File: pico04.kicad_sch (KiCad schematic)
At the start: 41 parts

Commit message: Place the footprint on the PCB
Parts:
- removed C? (x4): 0.1uF, symbol Device:C_Small
- removed UGRGB? (x4): WS2812B, LED_SMD:LED_WS2812B_PLCC4_5.0x5.0mm_P3.2mm, symbol LED:WS2812B
- C1: renamed from C?; footprint (none) -> Capacitor_SMD:C_0805_2012Metric
- CRGB1, CRGB2, CRGB3, CRGB4: renamed from C?; footprint (none) -> Capacitor_SMD:C_0603_1608Metric
- D1, D2, D3, D4: renamed from D?; footprint (none) -> Diode_SMD:D_SOD-123
- MX1, MX2, MX3, MX4: renamed from MX?; footprint (none) -> Pico04:MXOnly-1U-Hotswap
- R3, R4, R5, R6: renamed from R?; footprint (none) -> Resistor_SMD:R_0805_2012Metric
- RGB1: renamed from RGB?; footprint LED_SMD:LED_WS2812B_PLCC4_5.0x5.0mm_P3.2mm -> Pico04:WS2812B-3528
- RGB2, RGB3, RGB4: renamed from D?; footprint LED_SMD:LED_WS2812B_PLCC4_5.0x5.0mm_P3.2mm -> Pico04:WS2812B-3528
- SW1: renamed from SW?; footprint (none) -> random-keyboard-parts.pretty:SKQGADE010
- U1: renamed from U?; footprint Random-keyboard-parts:SOT143B -> random-keyboard-parts.pretty:SOT143B
- gave numbers to parts that had none: 10
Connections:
- net GND: now also CRGB1.2, CRGB2.2, CRGB3.2, CRGB4.2
- no-connect marks 4 -> 3

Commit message: Complete the PCB
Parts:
- renumbered D3 to D1, D4 to D2, D1 to D3, D2 to D4, MX3 to MX1, MX4 to MX2, MX1 to MX3, MX2 to MX4
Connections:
- net COL0: now also U2.22 (PC7)
- net COL1: now also U2.9 (PD3)
- net ROW0: now also D1.1 (K), D2.1 (K), U2.25 (PC5); no longer D3.1 (K), D4.1 (K)
- net ROW1: now also D3.1 (K), D4.1 (K), U2.16 (PB2); no longer D1.1 (K), D2.1 (K)
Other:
- moved on the sheet: D1, D2, D3, D4, MX1, MX2, MX3, MX4
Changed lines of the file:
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@@
   (junction (at 241.3 31.75))
   (junction (at 260.35 31.75))
+  (no_connect (at 242.57 123.19))
   (no_connect (at 58.42 44.45))
-  (no_connect (at 242.57 123.19))
   (no_connect (at 58.42 29.21))
   (wire (pts (xy 46.355 79.375) (xy 46.355 83.185))
@@
     (effects (font (size 1.27 1.27)) (justify right))
   )
+  (global_label "ROW1" (shape input) (at 191.135 39.37 0)
+    (effects (font (size 1.27 1.27)) (justify left))
+  )
   (global_label "RGBLED" (shape input) (at 191.135 41.91 0)
     (effects (font (size 1.27 1.27)) (justify left))
   )
+  (global_label "ROW0" (shape input) (at 191.135 62.23 0)
+    (effects (font (size 1.27 1.27)) (justify left))
+  )
+  (global_label "COL0" (shape input) (at 191.135 67.31 0)
+    (effects (font (size 1.27 1.27)) (justify left))
+  )
+  (global_label "COL1" (shape input) (at 191.135 80.01 0)
+    (effects (font (size 1.27 1.27)) (justify left))
+  )
   (global_label "ROW0" (shape input) (at 228.6 44.45 180)
     (effects (font (size 1.27 1.27)) (justify right))
@@
   )
   (symbol (lib_id "power:GND") (at 234.95 134.62 0) (unit 1)
-    (property "Reference" "#PWR?" (id 0) (at 234.95 140.97 0)
+    (property "Reference" "#PWR0116" (id 0) (at 234.95 140.97 0)
       (effects (font (size 1.27 1.27)) hide)
     )
@@
   )
   (symbol (lib_id "Device:D_Small") (at 231.775 40.64 90) (unit 1)
-    (property "Reference" "D1" (id 0) (at 233.5531 39.4906 90)
+    (property "Reference" "D1" (id 0) (at 233.553 39.491 90)
       (effects (font (size 1.27 1.27)) (justify right))
     )
@@
   )
   (symbol (lib_id "Device:D_Small") (at 231.775 59.69 90) (unit 1)
-    (property "Reference" "D3" (id 0) (at 233.5531 58.5406 90)
+    (property "Reference" "D3" (id 0) (at 233.553 58.541 90)
       (effects (font (size 1.27 1.27)) (justify right))
     )
@@
   )
   (symbol (lib_id "Device:D_Small") (at 250.825 40.64 90) (unit 1)
-    (property "Reference" "D2" (id 0) (at 252.6031 39.4906 90)
+    (property "Reference" "D2" (id 0) (at 252.603 39.491 90)
       (effects (font (size 1.27 1.27)) (justify right))
     )
@@
   )
   (symbol (lib_id "Device:D_Small") (at 250.825 59.69 90) (unit 1)
-    (property "Reference" "D4" (id 0) (at 252.6031 58.5406 90)
+    (property "Reference" "D4" (id 0) (at 252.603 58.541 90)
       (effects (font (size 1.27 1.27)) (justify right))
     )
@@
   )
   (symbol (lib_id "MX_Alps_Hybrid:MX-NoLED") (at 237.49 33.02 0) (unit 1)
-    (property "Reference" "MX1" (id 0) (at 238.3755 27.4192 0)
+    (property "Reference" "MX1" (id 0) (at 238.375 27.419 0)
       (effects (font (size 1.524 1.524)))
     )
@@
   )
   (symbol (lib_id "MX_Alps_Hybrid:MX-NoLED") (at 237.49 52.07 0) (unit 1)
-    (property "Reference" "MX3" (id 0) (at 238.3755 46.4692 0)
+    (property "Reference" "MX3" (id 0) (at 238.375 46.469 0)
       (effects (font (size 1.524 1.524)))
     )
@@
   )
   (symbol (lib_id "MX_Alps_Hybrid:MX-NoLED") (at 256.54 33.02 0) (unit 1)
-    (property "Reference" "MX2" (id 0) (at 257.4255 27.4192 0)
+    (property "Reference" "MX2" (id 0) (at 257.425 27.419 0)
       (effects (font (size 1.524 1.524)))
     )
@@
   )
   (symbol (lib_id "MX_Alps_Hybrid:MX-NoLED") (at 256.54 52.07 0) (unit 1)
-    (property "Reference" "MX4" (id 0) (at 257.4255 46.4692 0)
+    (property "Reference" "MX4" (id 0) (at 257.425 46.469 0)
       (effects (font (size 1.524 1.524)))
     )
@@
     )
     (path "/1d2d9655-11b9-43b8-8ab6-612e24aa6fec"
-      (reference "#PWR?") (unit 1)
+      (reference "#PWR0116") (unit 1)
     )
     (path "/26bfde33-3b17-4dfa-b632-b75632d47ae7"
@@
       (reference "CRGB4") (unit 1)
     )
+    (path "/bd4ab8ad-2f65-4d8a-8d0d-c0821e4954a4"
+      (reference "D1") (unit 1)
+    )
+    (path "/40e942c4-856f-4481-9752-16af2cfdf79c"
+      (reference "D2") (unit 1)
+    )
     (path "/3ff054c0-d21f-48f0-bf05-8c876ae67903"
-      (reference "D1") (unit 1)
+      (reference "D3") (unit 1)
     )
     (path "/25c6b1f6-bc0a-40f6-83d3-4b08379c2571"
-      (reference "D2") (unit 1)
-    )
-    (path "/bd4ab8ad-2f65-4d8a-8d0d-c0821e4954a4"
-      (reference "D3") (unit 1)
-    )
-    (path "/40e942c4-856f-4481-9752-16af2cfdf79c"
       (reference "D4") (unit 1)
     )
@@
       (reference "F1") (unit 1)
     )
+    (path "/cea816e9-fe33-478f-83b6-8714a776833b"
+      (reference "MX1") (unit 1)
+    )
+    (path "/d35a3ce5-ec9f-41d8-9163-6e0433cc9ea7"
+      (reference "MX2") (unit 1)
+    )
     (path "/74801bab-9abf-47a8-a68b-5b4028d688b4"
-      (reference "MX1") (unit 1)
+      (reference "MX3") (unit 1)
     )
     (path "/de405e8f-3a87-4ab0-b6fb-c3378cb8c0db"
-      (reference "MX2") (unit 1)
-    )
-    (path "/cea816e9-fe33-478f-83b6-8714a776833b"
-      (reference "MX3") (unit 1)
-    )
-    (path "/d35a3ce5-ec9f-41d8-9163-6e0433cc9ea7"
       (reference "MX4") (unit 1)
     )

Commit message: Add some 3d models to the PCB
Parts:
- F1: footprint Fuse:Fuse_1206_3216Metric -> Pico04:Fuse_1206_3216Metric
- USB1: footprint Type-C:HRO-TYPE-C-31-M-12 -> Pico04:HRO-TYPE-C-31-M-12
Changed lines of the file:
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@@
   (junction (at 260.35 31.75))
   (no_connect (at 242.57 123.19))
+  (no_connect (at 58.42 29.21))
   (no_connect (at 58.42 44.45))
-  (no_connect (at 58.42 29.21))
   (wire (pts (xy 46.355 79.375) (xy 46.355 83.185))
     (stroke (width 0) (type solid) (color 0 0 0 0))
@@
     (property "Reference" "F1" (id 0) (at 89.535 21.5708 90))
     (property "Value" "500mA" (id 1) (at 89.535 23.87 90))
-    (property "Footprint" "Fuse:Fuse_1206_3216Metric" (id 2) (at 94.615 25.4 0)
+    (property "Footprint" "Pico04:Fuse_1206_3216Metric" (id 2) (at 94.615 25.4 0)
       (effects (font (size 1.27 1.27)) (justify left) hide)
     )
@@
       (effects (font (size 1.524 1.524)))
     )
-    (property "Footprint" "Type-C:HRO-TYPE-C-31-M-12" (id 2) (at 55.88 38.1 0)
-      (effects (font (size 1.524 1.524)) hide)
-    )
+    (property "Footprint" "Pico04:HRO-TYPE-C-31-M-12" (id 2) (at 55.88 38.1 0)
+      (effects (font (size 1.524 1.524)) hide)
+    )

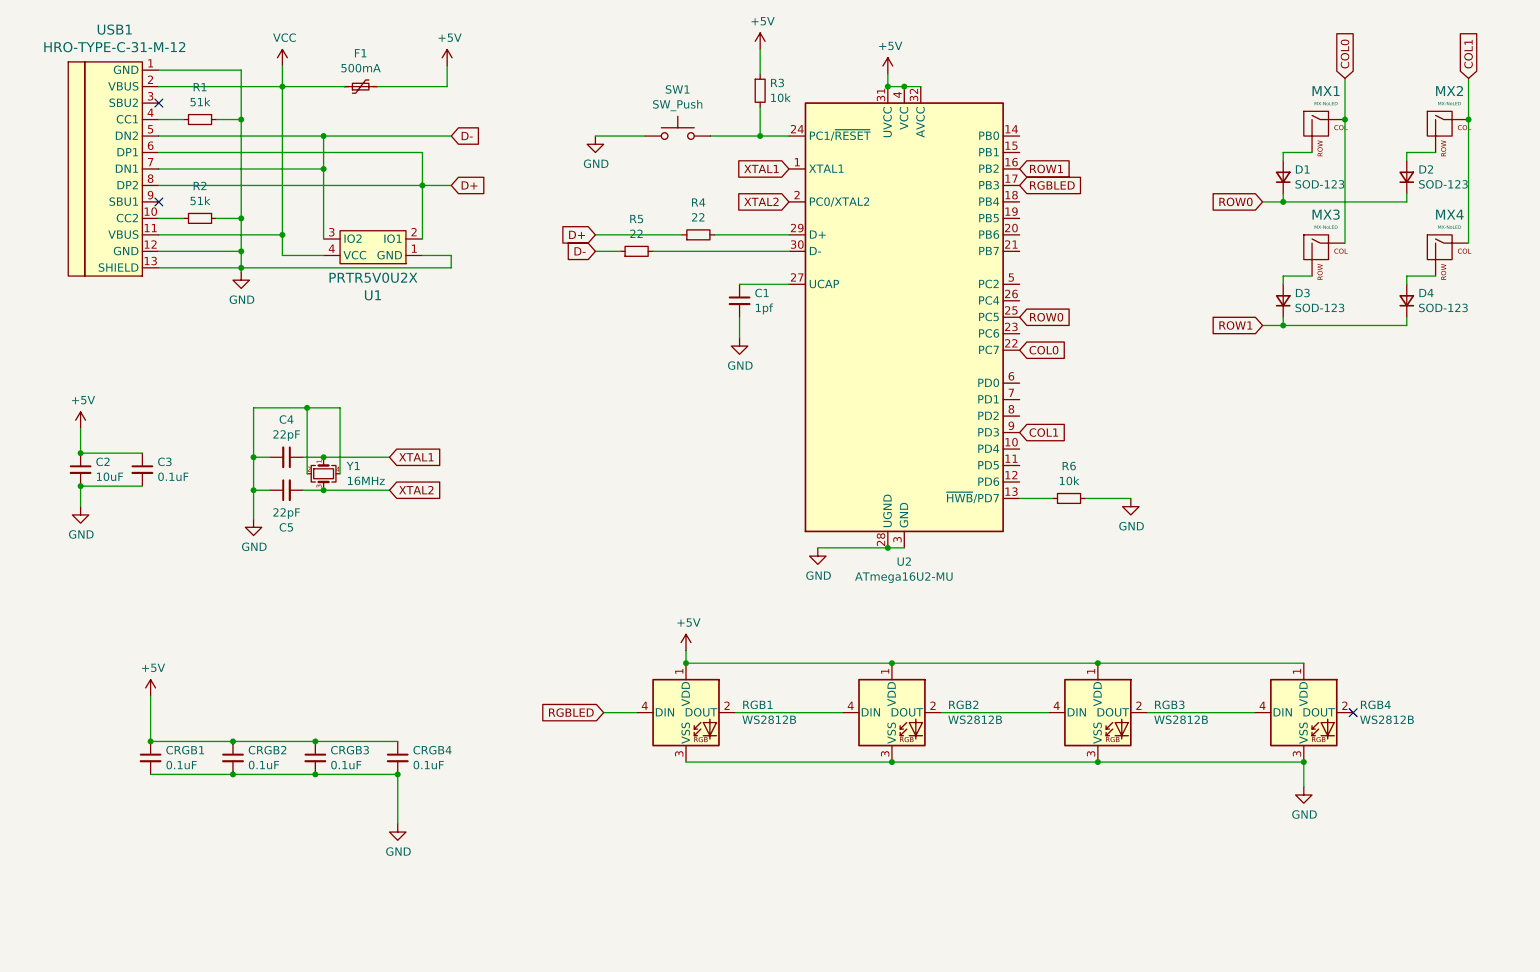
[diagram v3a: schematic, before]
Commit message: Re-route the PCB
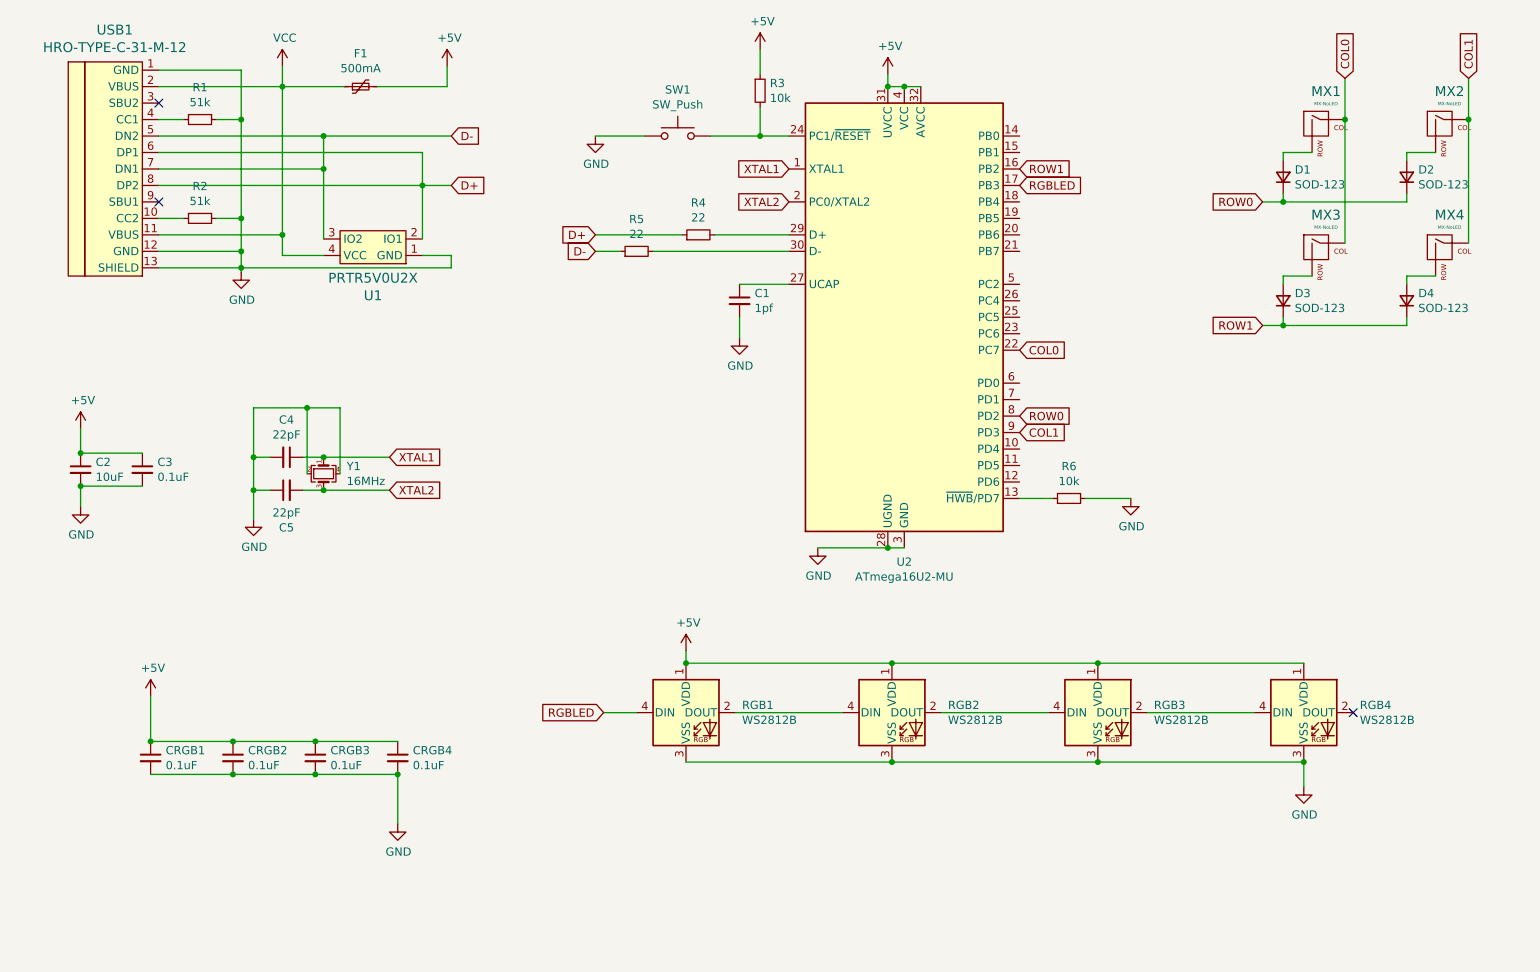
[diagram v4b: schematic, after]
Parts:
- renumbered CRGB3 to CRGB1, CRGB1 to CRGB2, CRGB2 to CRGB3, RGB3 to RGB1, RGB4 to RGB2, RGB1 to RGB3, RGB2 to RGB4
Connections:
- net RGBLED: now also RGB1.4 (DIN); no longer RGB3.4 (DIN)
- net ROW0: now also U2.8 (PD2); no longer U2.25 (PC5)
- net at RGB2.2 (DOUT): now also RGB3.4 (DIN)
- net at RGB4.2 (DOUT): no longer RGB1.4 (DIN)
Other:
- moved on the sheet: CRGB1, CRGB2, CRGB3, RGB1, RGB2, RGB3, RGB4
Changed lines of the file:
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@@
   (junction (at 241.3 31.75))
   (junction (at 260.35 31.75))
+  (no_connect (at 58.42 29.21))
   (no_connect (at 242.57 123.19))
-  (no_connect (at 58.42 29.21))
   (no_connect (at 58.42 44.45))
   (wire (pts (xy 46.355 79.375) (xy 46.355 83.185))
@@
     (stroke (width 0) (type solid) (color 0 0 0 0))
   )
+  (wire (pts (xy 57.15 132.715) (xy 69.85 132.715))
+    (stroke (width 0) (type solid) (color 0 0 0 0))
+  )
   (wire (pts (xy 58.42 24.13) (xy 71.12 24.13))
     (stroke (width 0) (type solid) (color 0 0 0 0))
@@
     (stroke (width 0) (type solid) (color 0 0 0 0))
   )
-  (wire (pts (xy 69.85 132.715) (xy 57.15 132.715))
+  (wire (pts (xy 69.85 132.715) (xy 82.55 132.715))
     (stroke (width 0) (type solid) (color 0 0 0 0))
   )
@@
     (stroke (width 0) (type solid) (color 0 0 0 0))
   )
-  (wire (pts (xy 82.55 132.715) (xy 69.85 132.715))
+  (wire (pts (xy 82.55 132.715) (xy 95.25 132.715))
     (stroke (width 0) (type solid) (color 0 0 0 0))
   )
@@
   )
   (wire (pts (xy 92.075 26.67) (xy 102.87 26.67))
-    (stroke (width 0) (type solid) (color 0 0 0 0))
-  )
-  (wire (pts (xy 95.25 132.715) (xy 82.55 132.715))
     (stroke (width 0) (type solid) (color 0 0 0 0))
   )
@@
     (effects (font (size 1.27 1.27)) (justify left))
   )
-  (global_label "ROW0" (shape input) (at 191.135 62.23 0)
+  (global_label "COL0" (shape input) (at 191.135 67.31 0)
     (effects (font (size 1.27 1.27)) (justify left))
   )
-  (global_label "COL0" (shape input) (at 191.135 67.31 0)
+  (global_label "ROW0" (shape input) (at 191.135 77.47 0)
     (effects (font (size 1.27 1.27)) (justify left))
   )
@@
       (reference "C5") (unit 1)
     )
+    (path "/d9825be5-035b-4657-aec7-0d08e2e89aa6"
+      (reference "CRGB1") (unit 1)
+    )
     (path "/3dd54350-3067-4efe-a0fe-53feda87da3f"
-      (reference "CRGB1") (unit 1)
+      (reference "CRGB2") (unit 1)
     )
     (path "/4c6b186c-719a-4471-8623-ed589bc596e2"
-      (reference "CRGB2") (unit 1)
-    )
-    (path "/d9825be5-035b-4657-aec7-0d08e2e89aa6"
       (reference "CRGB3") (unit 1)
     )
@@
       (reference "R6") (unit 1)
     )
+    (path "/91570c5a-fb32-4650-b2f9-ffa7d38ce130"
+      (reference "RGB1") (unit 1)
+    )
+    (path "/6fc1c3c7-e8a4-4e61-9814-224857e3a7ab"
+      (reference "RGB2") (unit 1)
+    )
     (path "/0c11f51b-50c9-4496-8a4f-32ce7c5ae082"
-      (reference "RGB1") (unit 1)
+      (reference "RGB3") (unit 1)
     )
     (path "/a1823596-5379-48ca-9e79-e27617d7fddd"
-      (reference "RGB2") (unit 1)
-    )
-    (path "/91570c5a-fb32-4650-b2f9-ffa7d38ce130"
-      (reference "RGB3") (unit 1)
-    )
-    (path "/6fc1c3c7-e8a4-4e61-9814-224857e3a7ab"
       (reference "RGB4") (unit 1)
     )
